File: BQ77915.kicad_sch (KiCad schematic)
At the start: 18 parts, among them U1 BQ7791500PWR

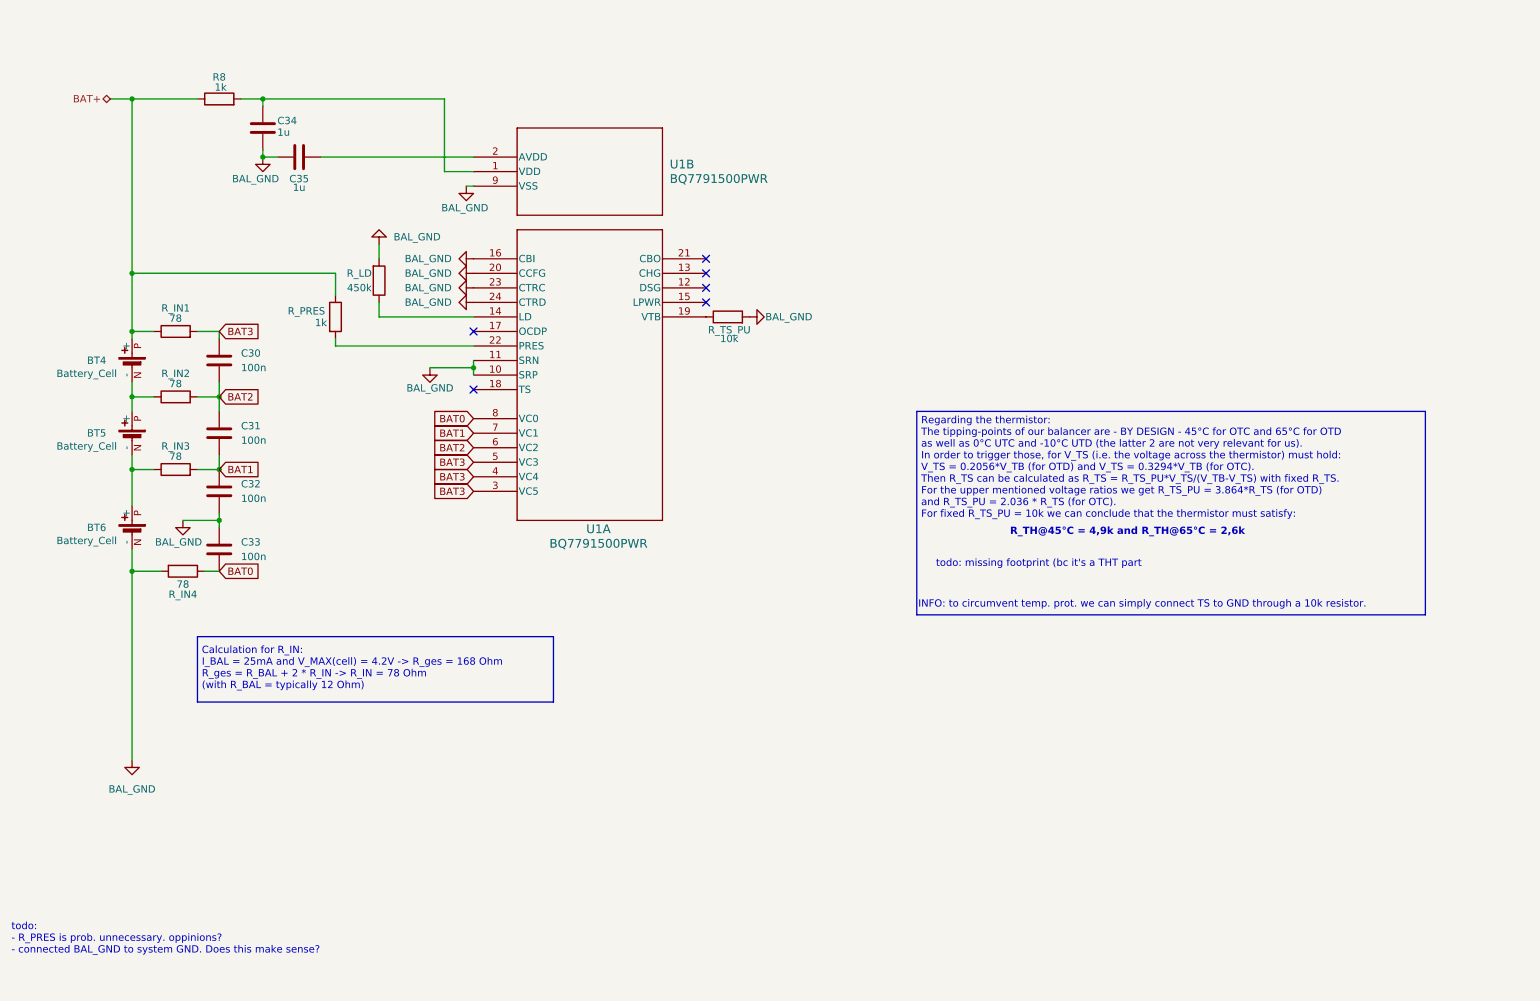
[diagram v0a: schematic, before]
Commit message: implemented changes according to errors found in the schematic design review (wip)
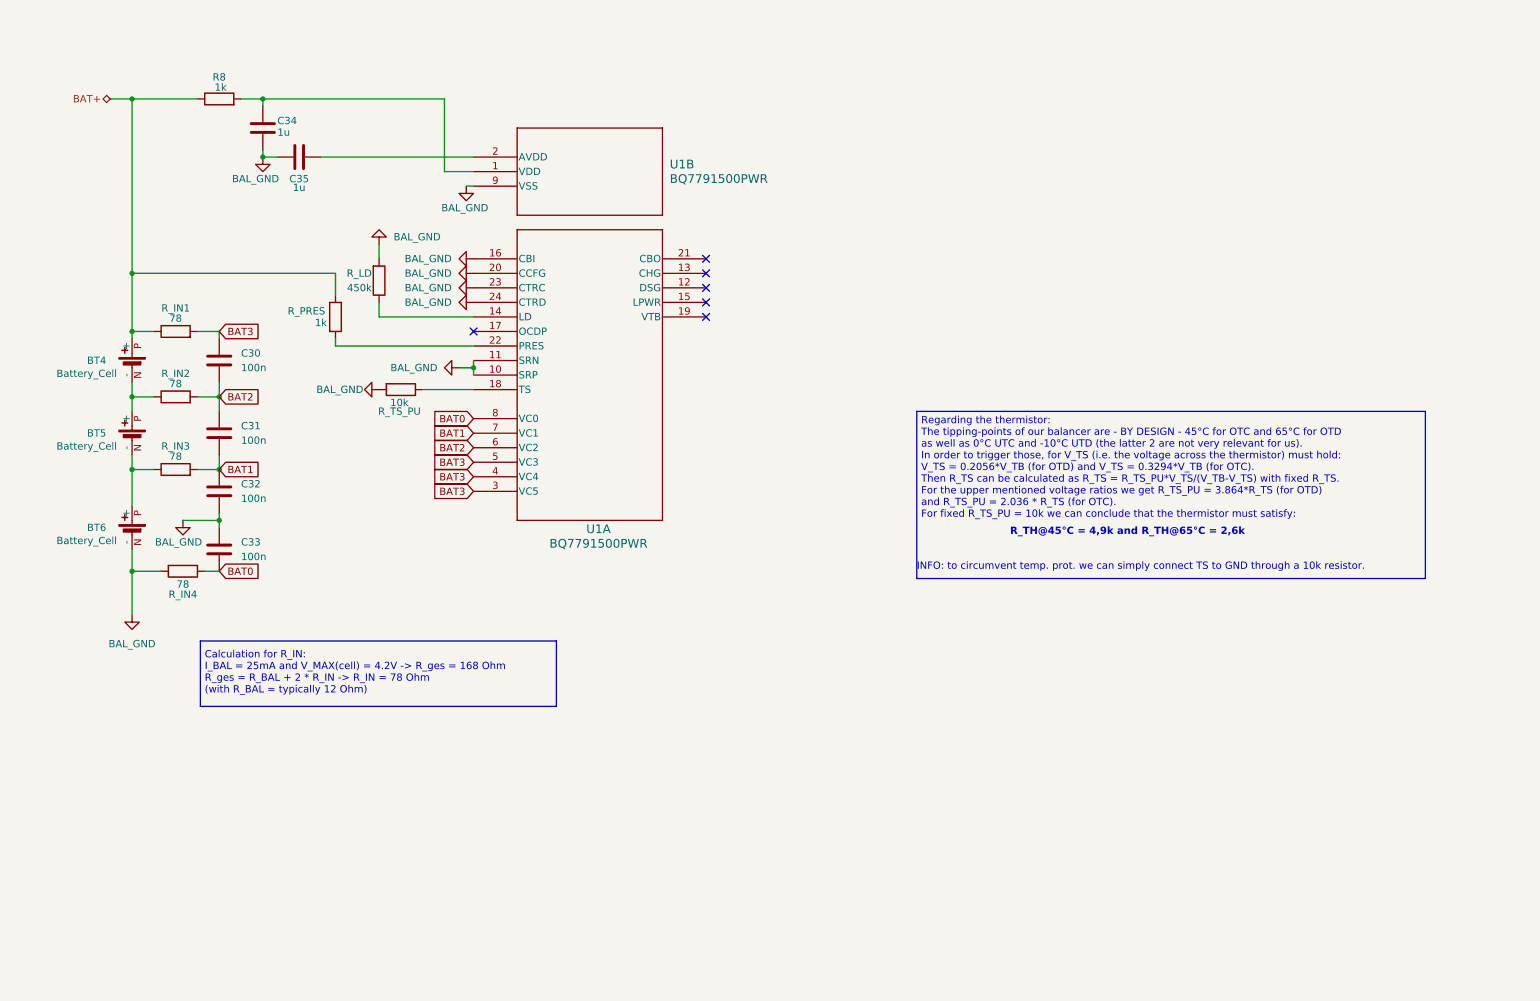
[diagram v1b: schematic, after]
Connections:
- net at R_TS_PU.1: now also U1.18 (TS); no longer U1.19 (VTB)
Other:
- note removed: "todo: - R_PRES is prob. unnecessary. oppinions? - connected BAL_GND to system GND. Does this make sense?"
- note removed: "todo: missing footprint (bc it's a THT part"
- moved on the sheet: R_TS_PU
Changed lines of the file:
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@@
 	(paper "A4")
 	(rectangle
-		(start 59.69 125.73)
-		(end 121.92 137.16)
+		(start 60.198 126.492)
+		(end 122.428 137.922)
 		(stroke
 			(width 0)
@@
 	(rectangle
 		(start 185.42 86.36)
-		(end 274.32 121.92)
+		(end 274.32 115.57)
 		(stroke
 			(width 0)
@@
 		(fill
 			(type none)
-		)
-	)
-	(text "todo: missing footprint (bc it's a THT part"
-		(exclude_from_sim no)
-		(at 206.756 113.03 0)
-		(effects
-			(font
-				(size 1.27 1.27)
-				(thickness 0.1588)
-			)
 		)
 	)
@@
 	(text "INFO: to circumvent temp. prot. we can simply connect TS to GND through a 10k resistor."
 		(exclude_from_sim no)
-		(at 185.674 120.142 0)
+		(at 185.42 113.538 0)
 		(effects
 			(font
@@
 	(text "Calculation for R_IN:\nI_BAL = 25mA and V_MAX(cell) = 4.2V -> R_ges = 168 Ohm\nR_ges = R_BAL + 2 * R_IN -> R_IN = 78 Ohm\n(with R_BAL = typically 12 Ohm)"
 		(exclude_from_sim no)
-		(at 60.452 131.318 0)
+		(at 60.96 132.08 0)
 		(effects
 			(font
@@
 		)
 	)
-	(text "todo:  \n- R_PRES is prob. unnecessary. oppinions?\n- connected BAL_GND to system GND. Does this make sense?\n"
-		(exclude_from_sim no)
-		(at 27.178 178.562 0)
-		(effects
-			(font
-				(size 1.27 1.27)
-			)
-			(justify left)
-		)
-	)
 	(junction
 		(at 63.5 96.52)
@@
 	)
 	(no_connect
+		(at 148.59 69.85)
+	)
+	(no_connect
 		(at 148.59 64.77)
 	)
-	(no_connect
-		(at 107.95 82.55)
-	)
 	(wire
 		(pts
@@
 	(wire
 		(pts
+			(xy 99.06 82.55) (xy 107.95 82.55)
+		)
+		(stroke
+			(width 0)
+			(type default)
+		)
+	)
+	(wire
+		(pts
 			(xy 48.26 96.52) (xy 52.07 96.52)
 		)
@@
 	(wire
 		(pts
-			(xy 100.33 78.74) (xy 107.95 78.74)
+			(xy 105.41 78.74) (xy 107.95 78.74)
 		)
 		(stroke
@@
 	(wire
 		(pts
-			(xy 48.26 114.3) (xy 48.26 147.32)
+			(xy 48.26 114.3) (xy 48.26 121.92)
 		)
 		(stroke
@@
 	(symbol
 		(lib_id "power:GND")
-		(at 156.21 69.85 90)
+		(at 91.44 82.55 270)
 		(unit 1)
 		(exclude_from_sim no)
@@
 		(dnp no)
 		(property "Reference" "#PWR051"
-			(at 162.56 69.85 0)
+			(at 85.09 82.55 0)
 			(effects
 				(font
@@
 		)
 		(property "Value" "BAL_GND"
-			(at 163.068 69.85 90)
+			(at 84.582 82.55 90)
 			(effects
 				(font
@@
 		)
 		(property "Footprint" ""
-			(at 156.21 69.85 0)
+			(at 91.44 82.55 0)
 			(effects
 				(font
@@
 		)
 		(property "Datasheet" ""
-			(at 156.21 69.85 0)
+			(at 91.44 82.55 0)
 			(effects
 				(font
@@
 		)
 		(property "Description" "Power symbol creates a global label with name \"GND\" , ground"
-			(at 156.21 69.85 0)
+			(at 91.44 82.55 0)
 			(effects
 				(font
@@
 	(symbol
 		(lib_id "Device:R")
-		(at 152.4 69.85 90)
+		(at 95.25 82.55 270)
 		(unit 1)
 		(exclude_from_sim no)
@@
 		(dnp no)
 		(property "Reference" "R_TS_PU"
-			(at 152.654 72.136 90)
+			(at 94.996 86.36 90)
 			(effects
 				(font
@@
 		)
 		(property "Value" "10k"
-			(at 152.654 73.66 90)
+			(at 94.996 84.836 90)
 			(effects
 				(font
@@
 		)
 		(property "Footprint" ""
-			(at 152.4 71.628 90)
+			(at 95.25 80.772 90)
 			(effects
 				(font
@@
 		)
 		(property "Datasheet" "~"
-			(at 152.4 69.85 0)
+			(at 95.25 82.55 0)
 			(effects
 				(font
@@
 		)
 		(property "Description" "Resistor"
-			(at 152.4 69.85 0)
+			(at 95.25 82.55 0)
 			(effects
 				(font
@@
 		)
 		(instances
-			(project ""
+			(project "rapid_power_module"
 				(path "/afc8cbd3-9ea8-40a2-afae-ed6bd0fe7e6e/f9ba2c7f-e63c-4860-86c8-ae922535c6b3"
 					(reference "R_TS_PU")
@@
 	(symbol
 		(lib_id "power:GND")
-		(at 48.26 147.32 0)
+		(at 48.26 121.92 0)
 		(unit 1)
 		(exclude_from_sim no)
@@
 		(fields_autoplaced yes)
 		(property "Reference" "#PWR045"
-			(at 48.26 153.67 0)
+			(at 48.26 128.27 0)
 			(effects
 				(font
@@
 		)
 		(property "Value" "BAL_GND"
-			(at 48.26 152.4 0)
+			(at 48.26 127 0)
 			(effects
 				(font
@@
 		)
 		(property "Footprint" ""
-			(at 48.26 147.32 0)
+			(at 48.26 121.92 0)
 			(effects
 				(font
@@
 		)
 		(property "Datasheet" ""
-			(at 48.26 147.32 0)
+			(at 48.26 121.92 0)
 			(effects
 				(font
@@
 		)
 		(property "Description" "Power symbol creates a global label with name \"GND\" , ground"
-			(at 48.26 147.32 0)
+			(at 48.26 121.92 0)
 			(effects
 				(font
@@
 	(symbol
 		(lib_id "power:GND")
-		(at 100.33 78.74 0)
+		(at 105.41 78.74 270)
 		(unit 1)
 		(exclude_from_sim no)
@@
 		(dnp no)
 		(property "Reference" "#PWR043"
-			(at 100.33 85.09 0)
+			(at 99.06 78.74 0)
 			(effects
 				(font
@@
 		)
 		(property "Value" "BAL_GND"
-			(at 100.33 82.296 0)
+			(at 97.536 78.74 90)
 			(effects
 				(font
@@
 		)
 		(property "Footprint" ""
-			(at 100.33 78.74 0)
+			(at 105.41 78.74 0)
 			(effects
 				(font
@@
 		)
 		(property "Datasheet" ""
-			(at 100.33 78.74 0)
+			(at 105.41 78.74 0)
 			(effects
 				(font
@@
 		)
 		(property "Description" "Power symbol creates a global label with name \"GND\" , ground"
-			(at 100.33 78.74 0)
-			(effects
-				(font
+			(at 105.41 78.74 0)
+			(effects
+				(font

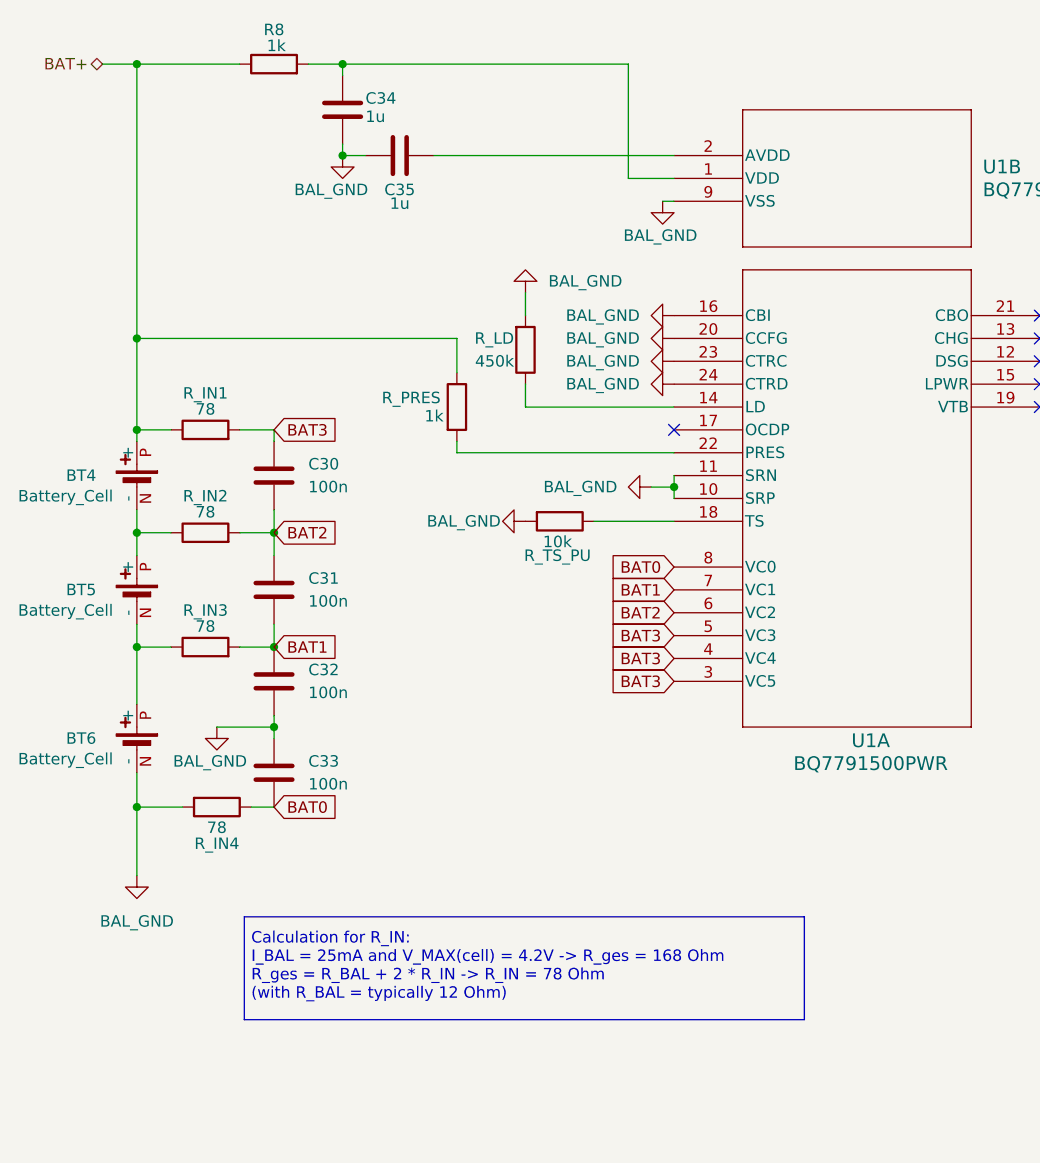
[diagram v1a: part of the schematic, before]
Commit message: added missing footprints and validated all lcsc numbers; started pcb-layouting
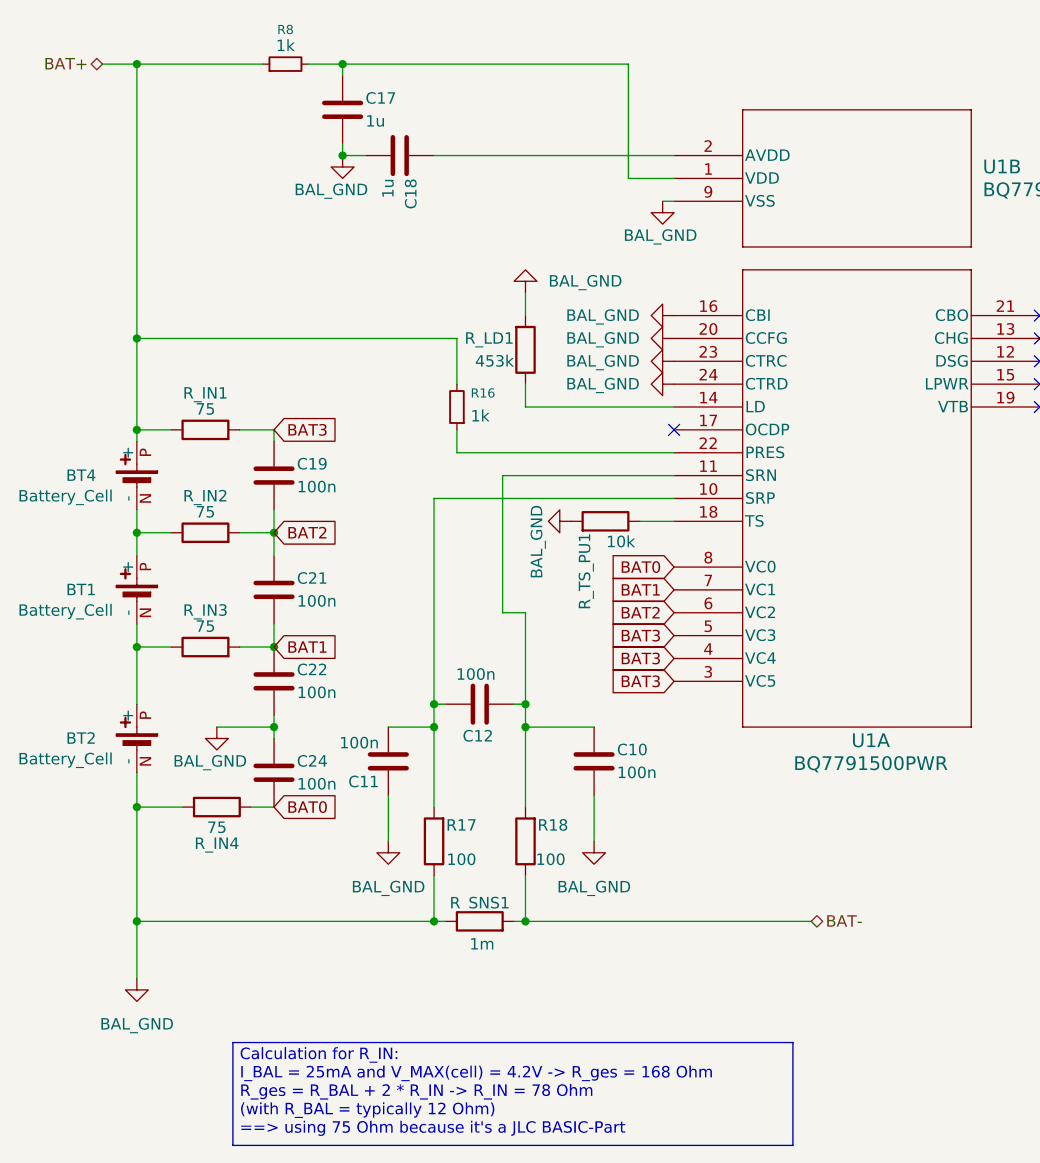
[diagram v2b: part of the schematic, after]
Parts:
- removed BT5, BT6: Battery_Cell, Inductor Wuerth:BAT_1043, symbol Device:Battery_Cell
- removed C30, C31, C32, C33: 100n, symbol Device:C
- removed C34, C35: 1u, symbol Device:C
- removed R8, R_PRES: 1k, symbol Device:R
- removed R_TS_PU: 10k, symbol Device:R
- added BT1, BT2: Battery_Cell, Inductor Wuerth:BAT_1043, symbol Device:Battery_Cell
- added C10, C11, C12, C19, C21, C22, C24: 100n, Capacitor_SMD:C_0402_1005Metric, symbol Device:C
- added C17, C18: 1u, Capacitor_SMD:C_0402_1005Metric, symbol Device:C
- added R16, R8: 1k, Resistor_SMD:R_0402_1005Metric, symbol Device:R_Small
- added R17, R18: 100, Resistor_SMD:R_0603_1608Metric, symbol Device:R
- added R_SNS1: 1m, Resistor_SMD:R_2512_6332Metric, symbol Device:R
- added R_TS_PU1: 10k, Resistor_SMD:R_0402_1005Metric, symbol Device:R
- BT4: LCSC (none) -> x
- R_IN1, R_IN2, R_IN3, R_IN4: value 78 -> 75; footprint (none) -> Resistor_SMD:R_0603_1608Metric; LCSC (none) -> C4275
- R_LD1: renamed from R_LD; value 450k -> 453k; footprint (none) -> Resistor_SMD:R_0402_1005Metric; LCSC (none) -> C27009
- U1: footprint PW24_TEX -> Package_SO:TSSOP-24_4.4x7.8mm_P0.65mm; LCSC (none) -> C2876946
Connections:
- net BAL_GND: now also BT2.N (-), C10.2, C11.1, C17.2, C18.2, C22.2, C24.1, R17.1, R_SNS1.1, R_TS_PU1.2; no longer U1.10 (SRP), U1.11 (SRN)
- net BAT+: now also R16.2, R8.1
- net BAT0: now also C24.2
- net BAT1: now also C21.2, C22.1
- net BAT2: now also C19.2, C21.1
- net BAT3: now also C19.1
- net at U1.1 (VDD): now also C17.1, R8.2
- net at U1.2 (AVDD): now also C18.1
- net at U1.18 (TS): now also R_TS_PU1.1
- net at R_IN3.1: now also BT1.N (-), BT2.P (+)
- net at BT4.N (-), R_IN2.1: now also BT1.P (+)
- net at U1.22 (PRES): now also R16.1
- new net: C11.2, C12.1, R17.2, U1.10 (SRP)
- new net: C10.1, C12.2, R18.2, U1.11 (SRN)
- new net BAT-: R18.1, R_SNS1.2
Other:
- note added: "Calculation for R_IN: I_BAL = 25mA and V_MAX(cell) = 4.2V -> R_ges = 168 Ohm R_ges = R_BAL + 2 * R_IN -> R_IN = 78 Ohm (with R_BAL = typically 12 Ohm) ==> using 75 Ohm because it's a JLC BASIC-Part"
- note removed: "Calculation for R_IN: I_BAL = 25mA and V_MAX(cell) = 4.2V -> R_ges = 168 Ohm R_ges = R_BAL + 2 * R_IN -> R_IN = 78 Ohm (with R_BAL = typically 12 Ohm)"

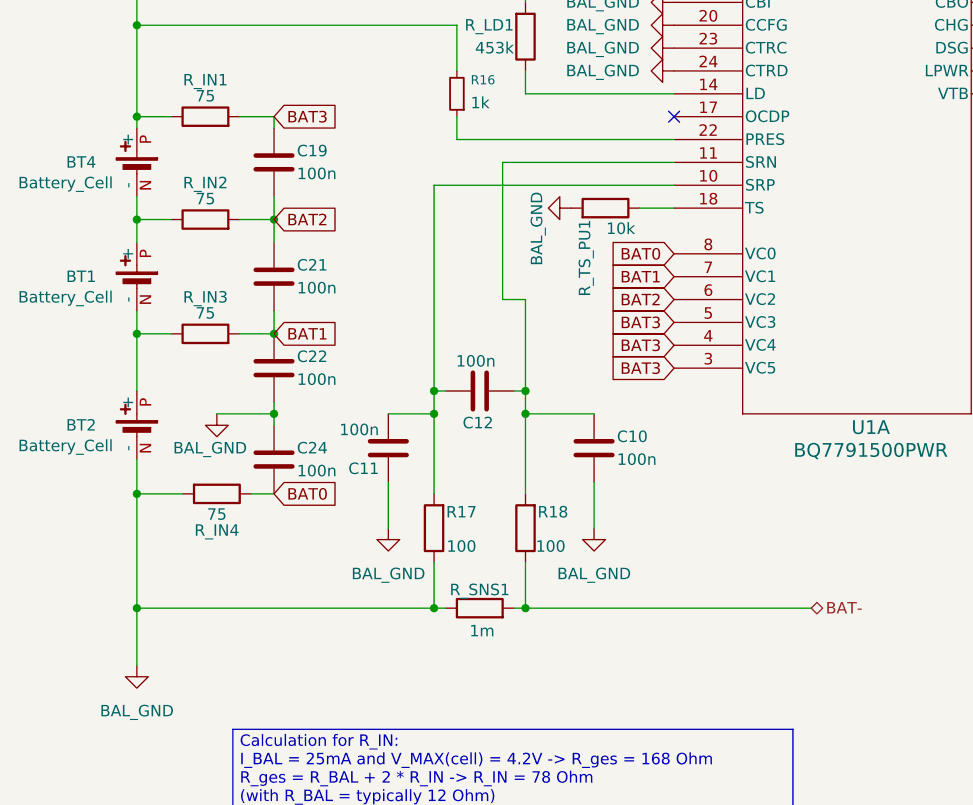
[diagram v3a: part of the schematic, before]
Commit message: implemented improvements based on feedback; Voltage/Current sensing still missing
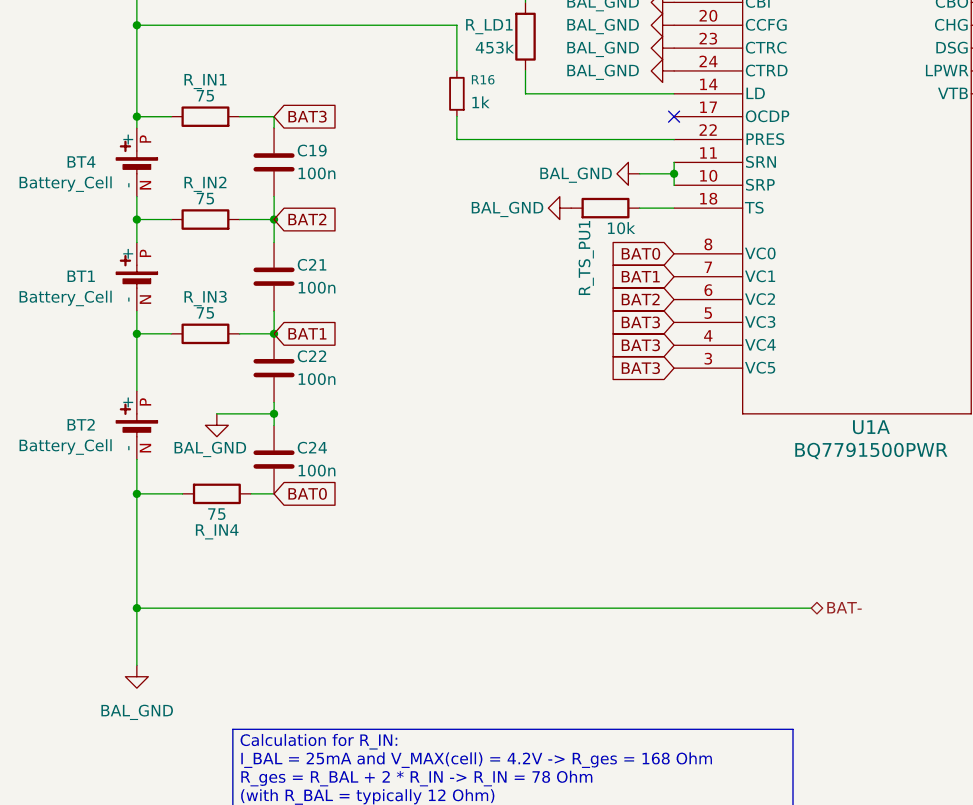
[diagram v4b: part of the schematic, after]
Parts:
- removed C10, C11, C12: 100n, Capacitor_SMD:C_0402_1005Metric, symbol Device:C
- removed R17, R18: 100, Resistor_SMD:R_0603_1608Metric, symbol Device:R
- removed R_SNS1: 1m, Resistor_SMD:R_2512_6332Metric, symbol Device:R
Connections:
- net BAL_GND: now also U1.10 (SRP), U1.11 (SRN)
